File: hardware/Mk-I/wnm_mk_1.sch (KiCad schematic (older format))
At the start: 34 parts, among them SW1 SW_PUSH, SW10 SW_PUSH, SW11 SW_PUSH, SW12 SW_PUSH, SW13 SW_PUSH, SW14 SW_PUSH, SW15 SW_PUSH, SW16 SW_PUSH, SW18 SW_PUSH, SW19 SW_PUSH, SW2 SW_PUSH, SW20 SW_PUSH, SW21 SW_PUSH, SW22 SW_PUSH, SW3 SW_PUSH, SW4 SW_PUSH, SW5 SW_PUSH, SW6 SW_PUSH, SW7 SW_PUSH, SW8 SW_PUSH, SW9 SW_PUSH, U6 encoder_and_switch, U7 encoder_and_switch

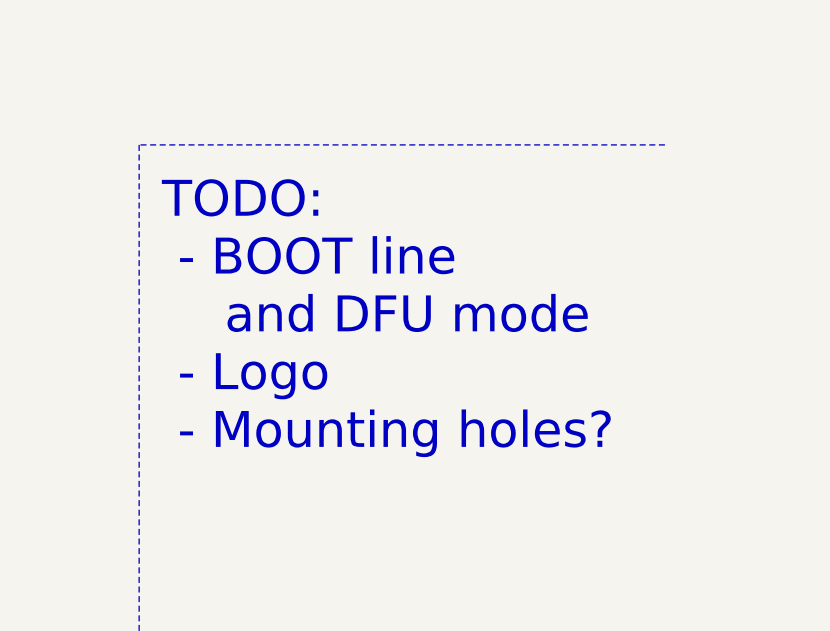
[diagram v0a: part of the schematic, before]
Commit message: Add mounting hole
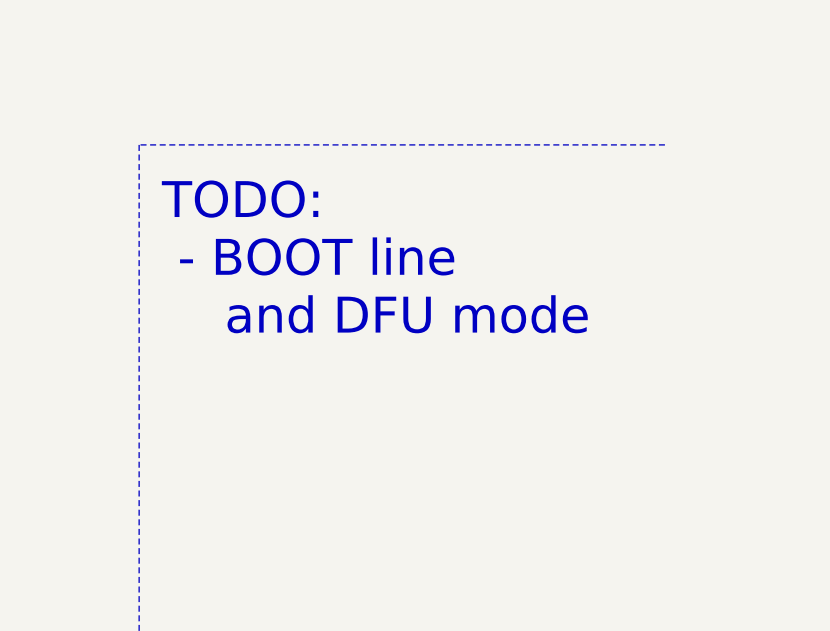
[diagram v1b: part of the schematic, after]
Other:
- note added: "TODO:\n - BOOT line \n and DFU mode"
- note removed: "TODO:\n - BOOT line \n and DFU mode\n - Logo\n - Mounting holes?"
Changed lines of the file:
@@
 F1 "audio.sch" 60
 $EndSheet
-Text Notes 8950 5450 0    157  ~ 0
-TODO:\n - BOOT line \n    and DFU mode\n - Logo\n - Mounting holes?
+Text Notes 8950 4950 0    157  ~ 0
+TODO:\n - BOOT line \n    and DFU mode
 Text GLabel 4850 5700 0    60   Input ~ 0
 WAKEUP

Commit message: HW: Add a DFU mode switch
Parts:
- C30, C31, C32, C33: symbol C -> C-RESCUE-wnm_mk_1
- R16, R17, R18, R19: symbol R -> R-RESCUE-wnm_mk_1
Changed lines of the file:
@@
 EESchema Schematic File Version 2
+LIBS:wnm_mk_1-rescue
 LIBS:power
 LIBS:device
@@
 LIBS:microchip_pic12mcu
 LIBS:microchip_pic16mcu
-LIBS:microchip1
 LIBS:msp430
 LIBS:nxp_armmcu
@@
 LIBS:relays
 LIBS:sensors
-LIBS:special
 LIBS:stm8
 LIBS:stm32
@@
 ENC_1_B
 $Comp
-L GND #PWR01
+L GND-RESCUE-wnm_mk_1 #PWR01
 U 1 1 586532D8
 P 4950 7050
@@
 $EndComp
 $Comp
-L GND #PWR02
+L GND-RESCUE-wnm_mk_1 #PWR02
 U 1 1 58653337
 P 2200 7050
@@
 	8000 3750 8000 5700
 $Comp
-L R R16
+L R-RESCUE-wnm_mk_1 R16
 U 1 1 58664AEC
 P 1700 7050
@@
 $EndComp
 $Comp
-L C C30
+L C-RESCUE-wnm_mk_1 C30
 U 1 1 58664DFD
 P 1450 7250
@@
 $EndComp
 $Comp
-L GND #PWR03
+L GND-RESCUE-wnm_mk_1 #PWR03
 U 1 1 58664E6F
 P 1450 7450
@@
 $EndComp
 $Comp
-L R R17
+L R-RESCUE-wnm_mk_1 R17
 U 1 1 586652D6
 P 2700 7050
@@
 $EndComp
 $Comp
-L C C31
+L C-RESCUE-wnm_mk_1 C31
 U 1 1 586655E8
 P 2950 7250
@@
 $EndComp
 $Comp
-L GND #PWR04
+L GND-RESCUE-wnm_mk_1 #PWR04
 U 1 1 5866566D
 P 2950 7450
@@
 ENC_2_B
 $Comp
-L R R19
+L R-RESCUE-wnm_mk_1 R19
 U 1 1 58665F22
 P 5450 7050
@@
 $EndComp
 $Comp
-L C C33
+L C-RESCUE-wnm_mk_1 C33
 U 1 1 58665F28
 P 5700 7250
@@
 $EndComp
 $Comp
-L GND #PWR05
+L GND-RESCUE-wnm_mk_1 #PWR05
 U 1 1 58665F2E
 P 5700 7450
@@
 ENC_2_A
 $Comp
-L R R18
+L R-RESCUE-wnm_mk_1 R18
 U 1 1 58666537
 P 4450 7050
@@
 $EndComp
 $Comp
-L C C32
+L C-RESCUE-wnm_mk_1 C32
 U 1 1 5866653D
 P 4200 7250
@@
 $EndComp
 $Comp
-L GND #PWR06
+L GND-RESCUE-wnm_mk_1 #PWR06
 U 1 1 58666543
 P 4200 7450

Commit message: HW: Update TODO list
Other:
- note added: "TODO:"
- note removed: "TODO:\n - BOOT line \n and DFU mode"
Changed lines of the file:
@@
 F1 "audio.sch" 60
 $EndSheet
-Text Notes 8950 4950 0    157  ~ 0
-TODO:\n - BOOT line \n    and DFU mode
 Text GLabel 4850 5700 0    60   Input ~ 0
 WAKEUP
@@
 	1    0    0    -1
 $EndComp
+Text Notes 8950 4400 0    157  ~ 0
+TODO:
 $EndSCHEMATC

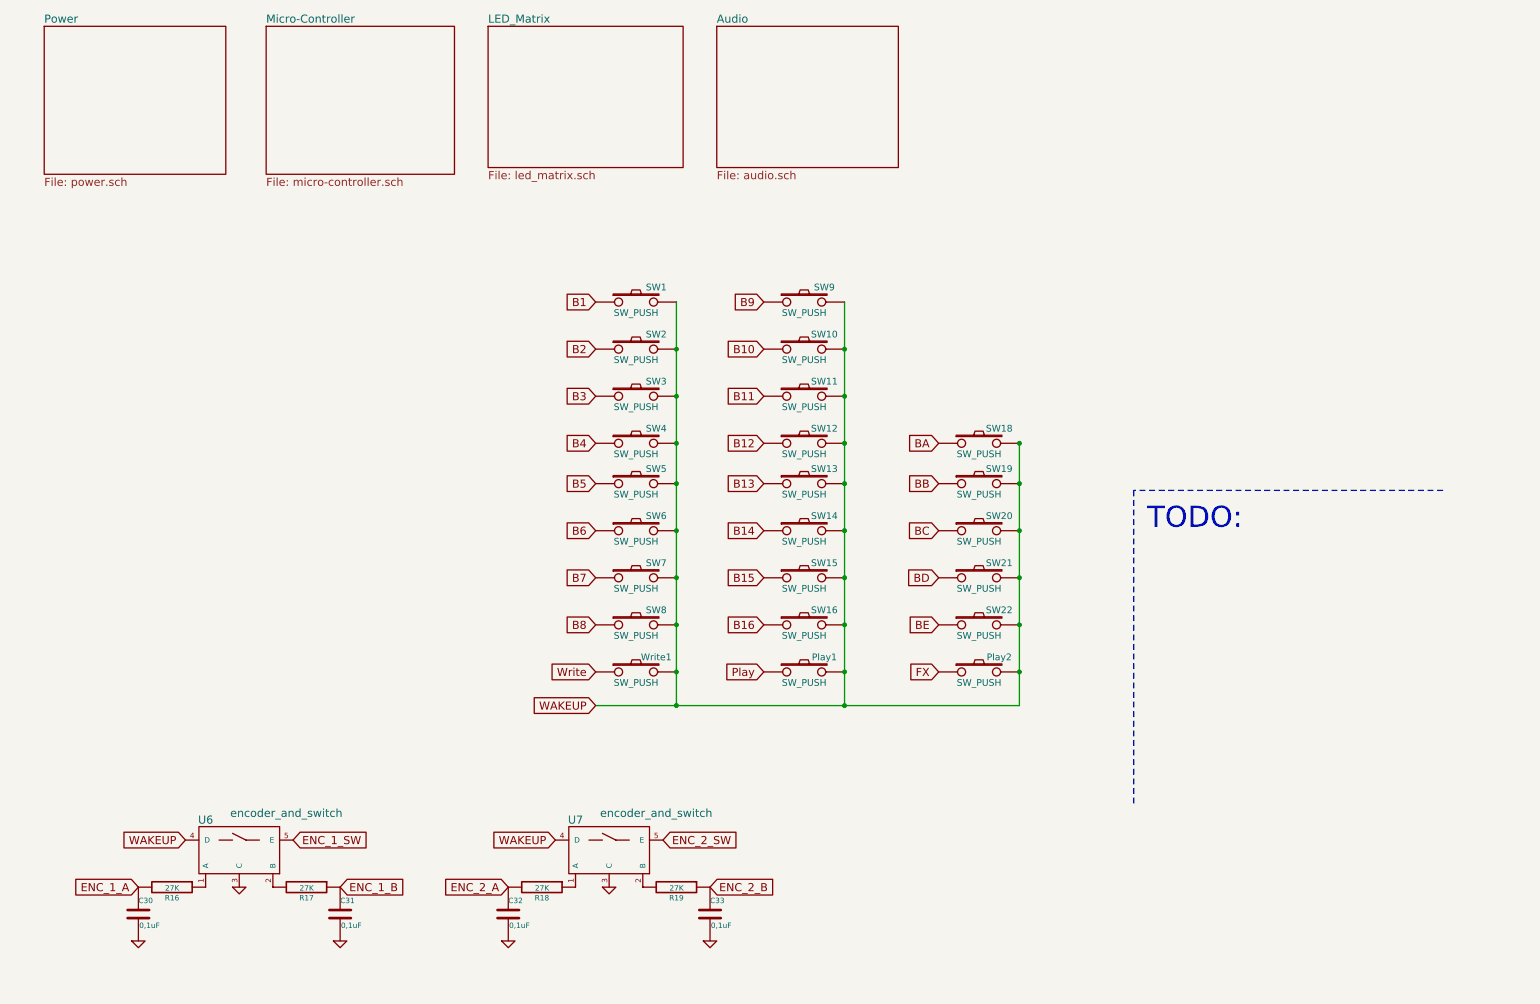
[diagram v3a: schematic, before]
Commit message: HW: Start Mk-I rev-A known problems
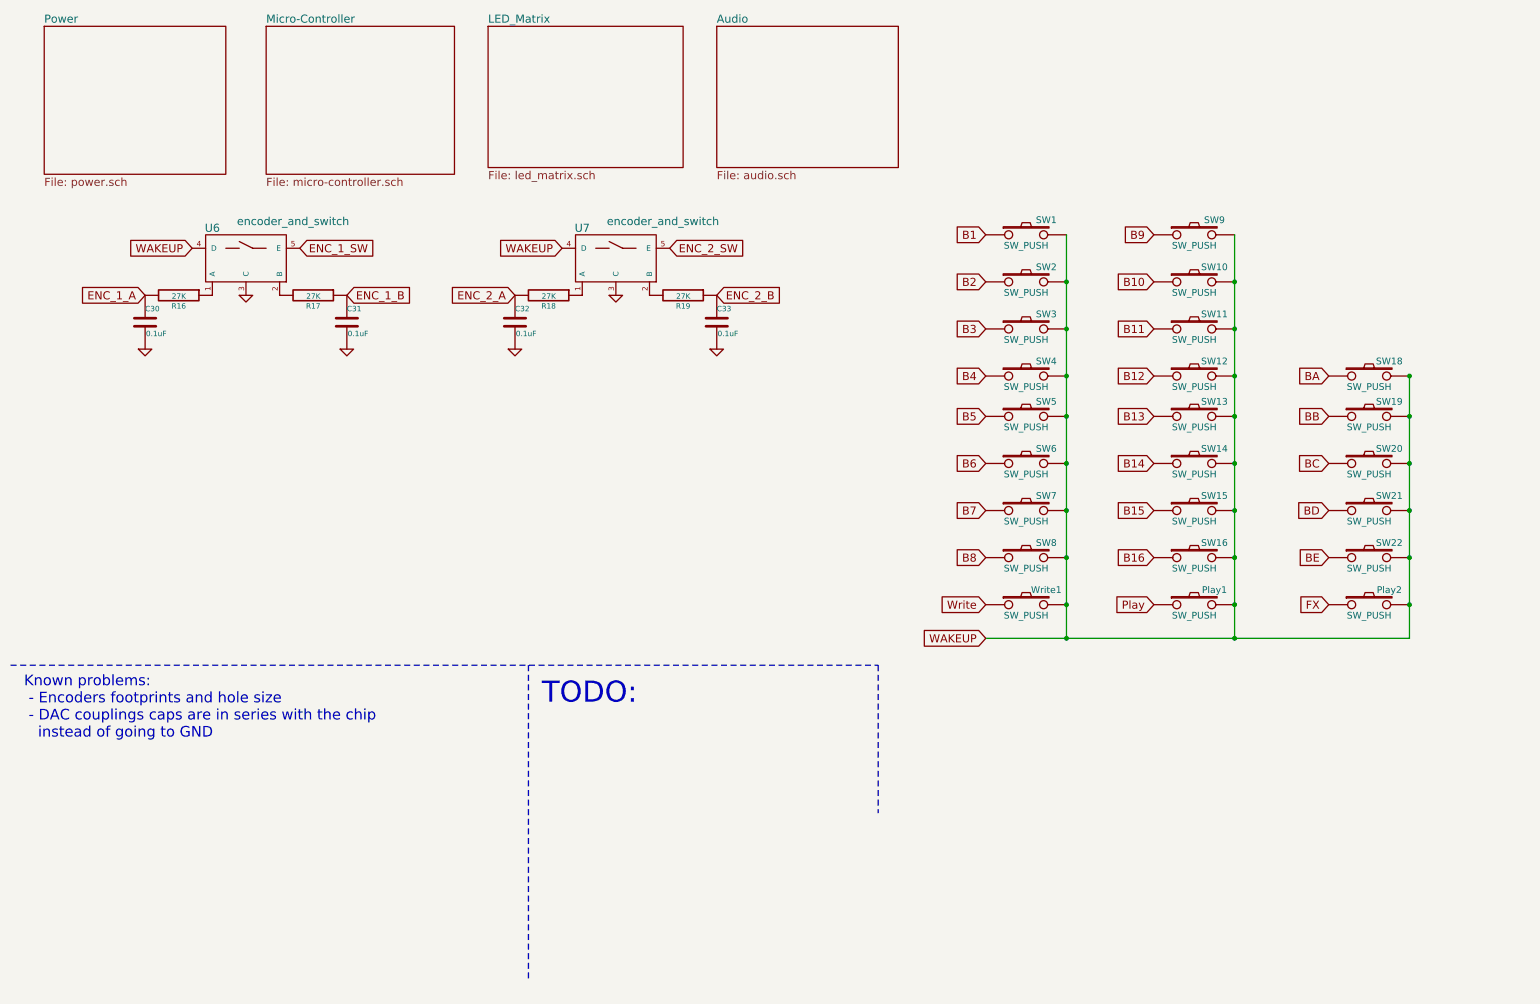
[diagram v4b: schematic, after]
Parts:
- C30, C31, C32, C33: value 0,1uF -> 0.1uF
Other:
- note added: "Known problems:\n - Encoders footprints and hole size\n - DAC couplings caps are in series with the chip \n instead of going to GND"
- moved on the sheet: C30, C31, C32, C33, Play1, Play2, R16, R17, R18, R19, SW1, SW10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

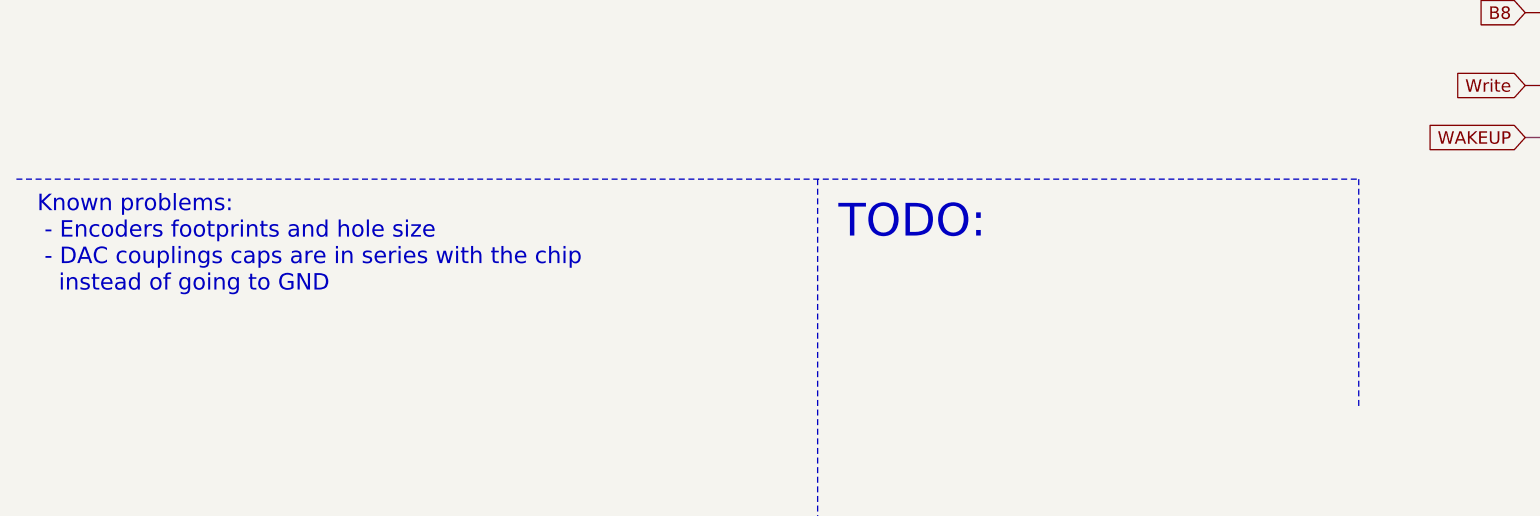
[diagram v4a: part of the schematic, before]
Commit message: HW: known problems cont.
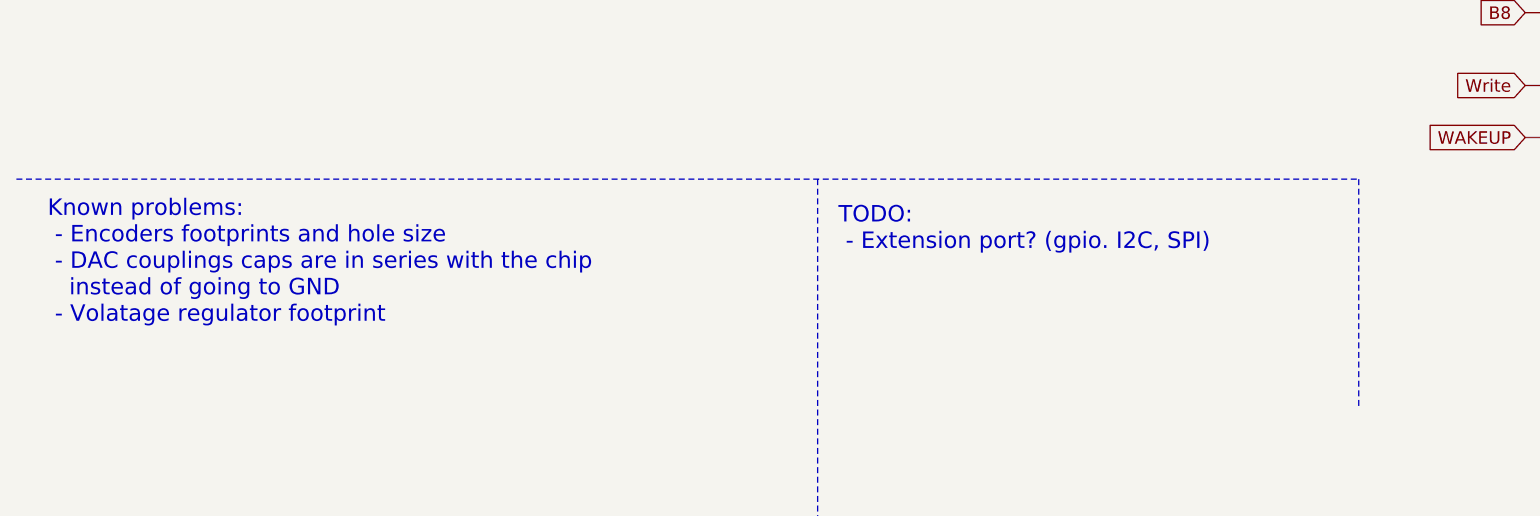
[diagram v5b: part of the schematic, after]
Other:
- note added: "Known problems:\n - Encoders footprints and hole size\n - DAC couplings caps are in series with the chip \n instead of going to GND\n - Volatage regulator footprint"
- note added: "TODO:\n - Extension port? (gpio. I2C, SPI)"
- note removed: "Known problems:\n - Encoders footprints and hole size\n - DAC couplings caps are in series with the chip \n instead of going to GND"
- note removed: "TODO:"
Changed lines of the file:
@@
 	1    0    0    -1
 $EndComp
-Text Notes 4450 5700 0    157  ~ 0
-TODO:
+Text Notes 4450 5750 0    79   ~ 0
+TODO:\n - Extension port? (gpio. I2C, SPI)
 Wire Notes Line
 	500  5400 6950 5400
 Wire Notes Line
 	6950 5400 6950 6500
-Text Notes 600  5950 0    79   ~ 0
-Known problems:\n - Encoders footprints and hole size\n - DAC couplings caps are in series with the chip \n   instead of going to GND
+Text Notes 650  6100 0    79   ~ 0
+Known problems:\n - Encoders footprints and hole size\n - DAC couplings caps are in series with the chip \n   instead of going to GND\n - Volatage regulator footprint
 $EndSCHEMATC

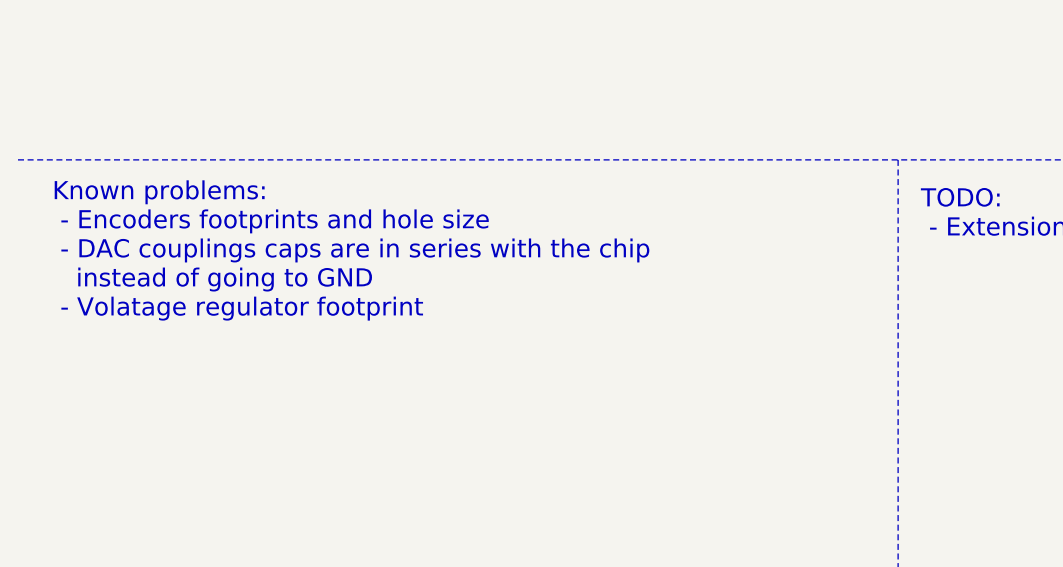
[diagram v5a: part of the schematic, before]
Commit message: HW: Fix DAC coupling caps
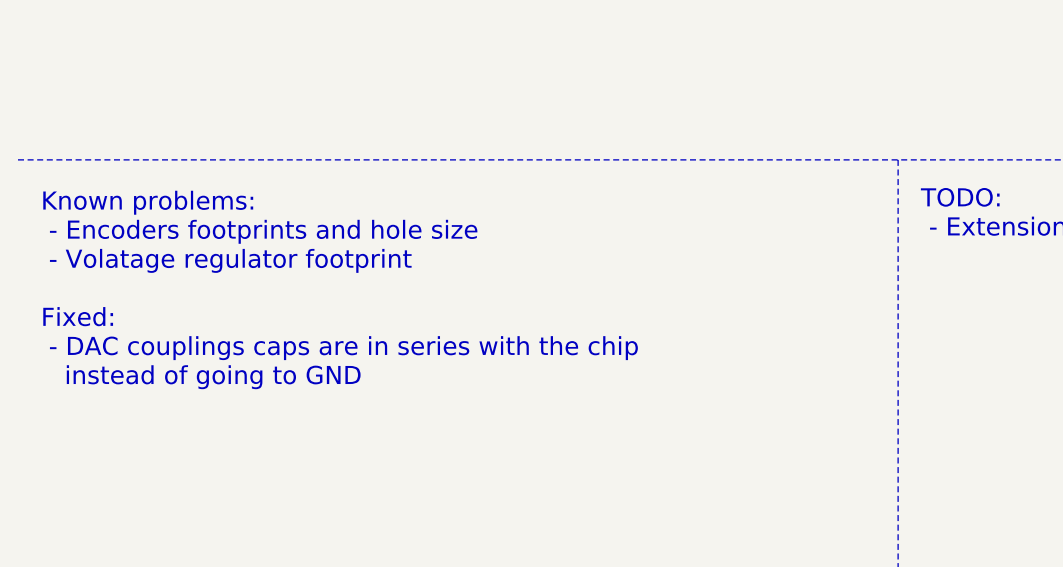
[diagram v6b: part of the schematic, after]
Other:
- note added: "Known problems:\n - Encoders footprints and hole size\n - Volatage regulator footprint\n\nFixed:\n - DAC couplings caps are in series with the chip \n instead of going to GND\n"
- note removed: "Known problems:\n - Encoders footprints and hole size\n - DAC couplings caps are in series with the chip \n instead of going to GND\n - Volatage regulator footprint"
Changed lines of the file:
@@
 Wire Notes Line
 	6950 5400 6950 6500
-Text Notes 650  6100 0    79   ~ 0
-Known problems:\n - Encoders footprints and hole size\n - DAC couplings caps are in series with the chip \n   instead of going to GND\n - Volatage regulator footprint
+Text Notes 600  6400 0    79   ~ 0
+Known problems:\n - Encoders footprints and hole size\n - Volatage regulator footprint\n\nFixed:\n - DAC couplings caps are in series with the chip \n   instead of going to GND\n
 $EndSCHEMATC

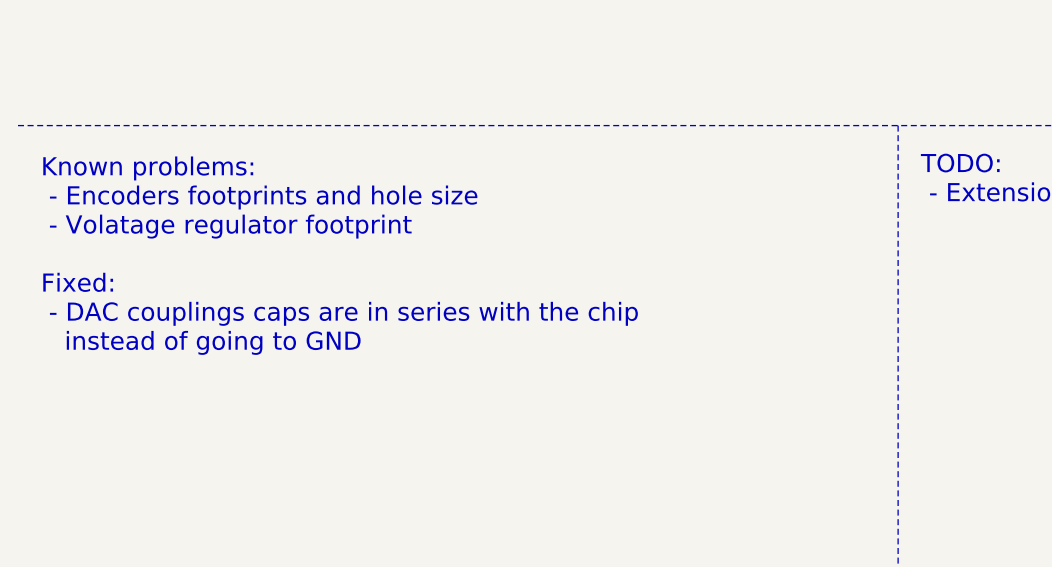
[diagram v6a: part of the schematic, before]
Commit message: HW: Fix regulator footprint
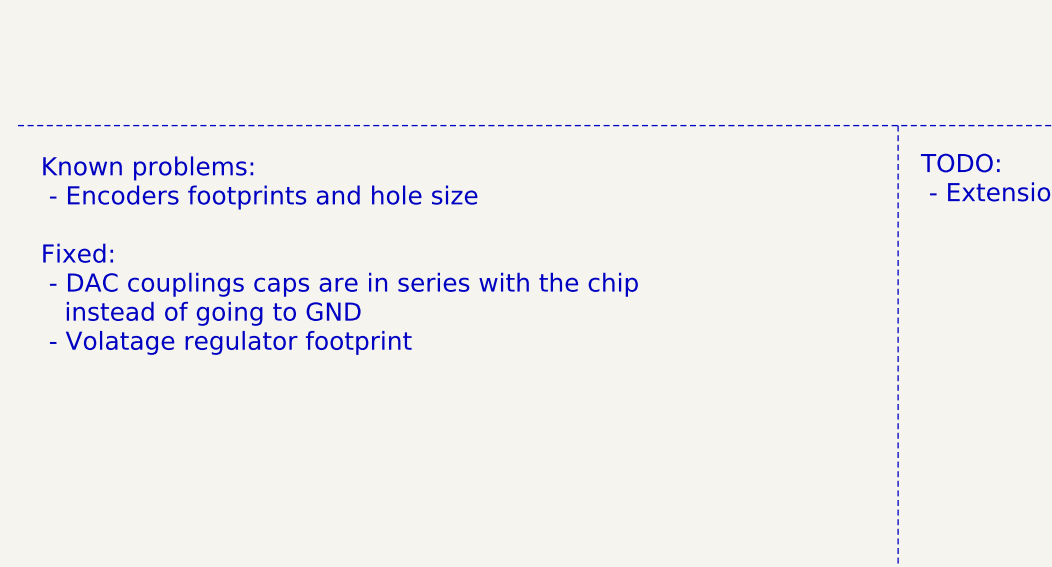
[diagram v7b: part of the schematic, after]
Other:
- note added: "Known problems:\n - Encoders footprints and hole size\n\nFixed:\n - DAC couplings caps are in series with the chip \n instead of going to GND\n - Volatage regulator footprint\n"
- note removed: "Known problems:\n - Encoders footprints and hole size\n - Volatage regulator footprint\n\nFixed:\n - DAC couplings caps are in series with the chip \n instead of going to GND\n"
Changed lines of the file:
@@
 	6950 5400 6950 6500
 Text Notes 600  6400 0    79   ~ 0
-Known problems:\n - Encoders footprints and hole size\n - Volatage regulator footprint\n\nFixed:\n - DAC couplings caps are in series with the chip \n   instead of going to GND\n
+Known problems:\n - Encoders footprints and hole size\n\nFixed:\n - DAC couplings caps are in series with the chip \n   instead of going to GND\n - Volatage regulator footprint\n
 $EndSCHEMATC
